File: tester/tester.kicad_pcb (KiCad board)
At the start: 2 copper layers, 29.8 x 91.4 mm, 70 parts

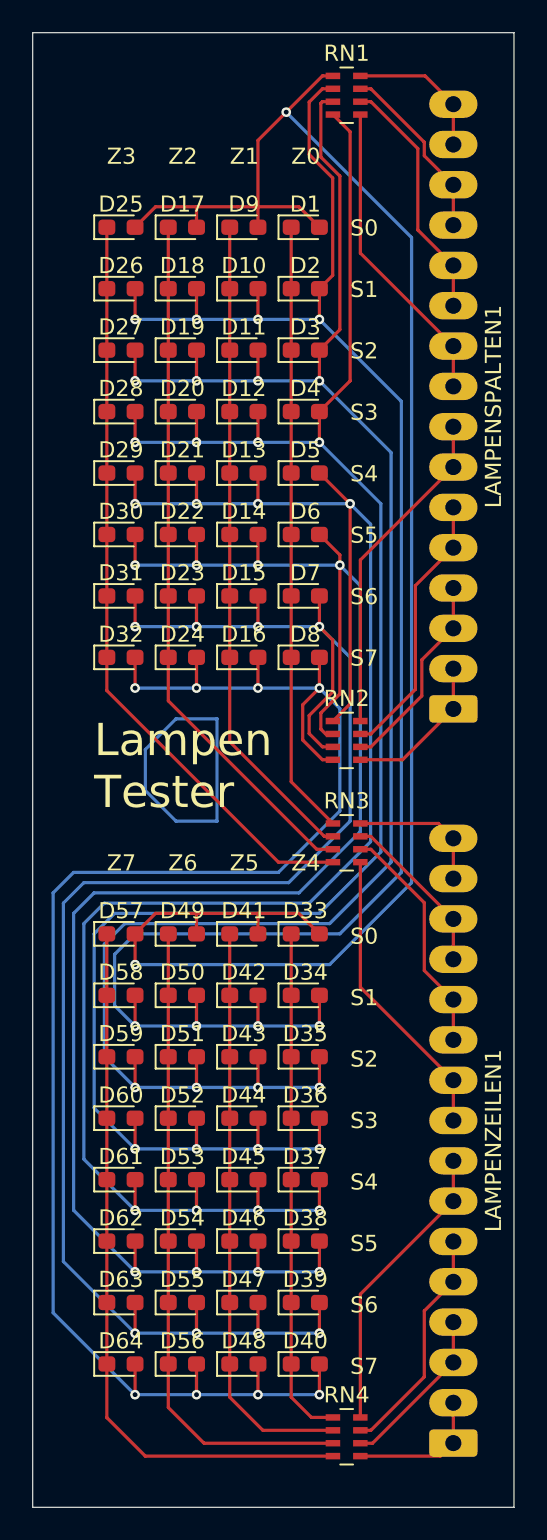
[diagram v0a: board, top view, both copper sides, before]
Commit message: led tester
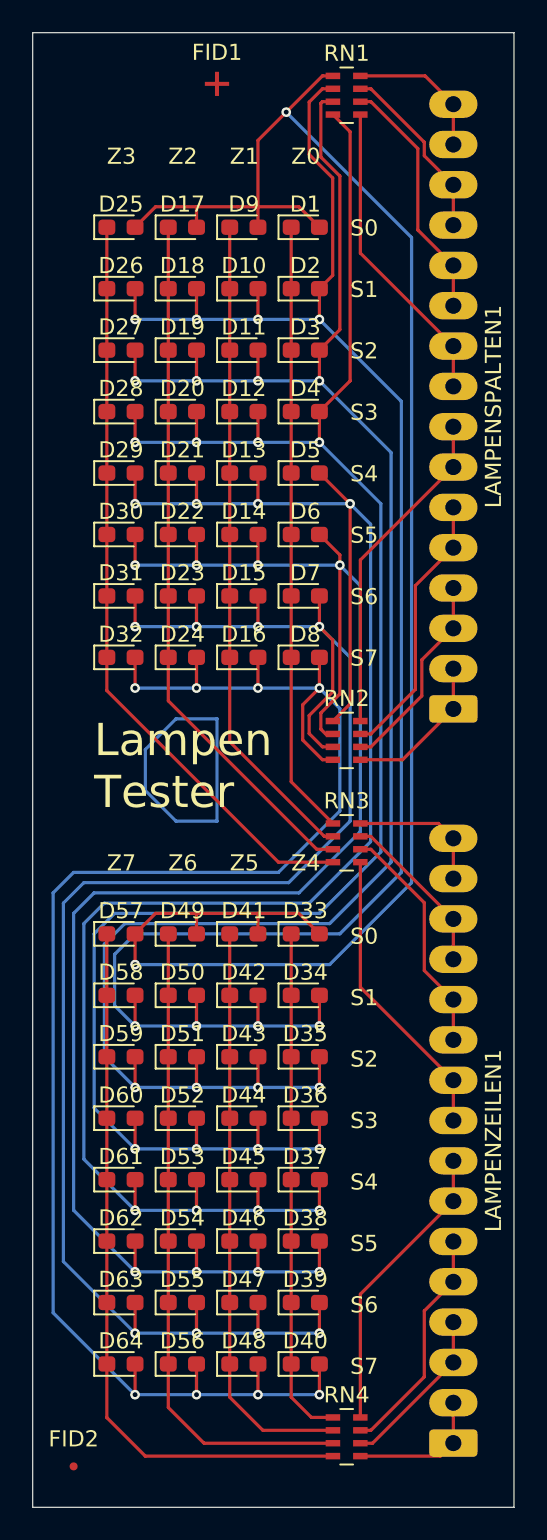
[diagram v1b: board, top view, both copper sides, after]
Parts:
- added FID1: Fiducial, Fiducial:Fiducial_Cross_1.5mm_Mask2mm, F.Cu at (49.5, 28.6)
- added FID2: Fiducial, Fiducial:Fiducial_0.5mm_Mask1.5mm, F.Cu at (40.6, 114.3)
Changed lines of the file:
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@@
 		)
+	)
+	(footprint "Fiducial:Fiducial_Cross_1.5mm_Mask2mm"
+		(layer "F.Cu")
+		(at 49.53 28.575)
+		(descr "Fiducial, cross variant, 1.5mm bare copper, 2mm soldermask opening")
+		(tags "fiducial")
+		(property "Reference" "FID1"
+			(at 0 -1.95 0)
+			(layer "F.SilkS")
+			(effects
+				(font
+					(size 1 1)
+					(thickness 0.15)
+				)
+			)
+		)
+		(property "Value" "Fiducial"
+			(at 0 1.95 0)
+			(layer "F.Fab")
+			(effects
+				(font
+					(size 1 1)
+					(thickness 0.15)
+				)
+			)
+		)
+		(property "Datasheet" "~"
+			(at 0 0 0)
+			(layer "F.Fab")
+			(hide yes)
+			(effects
+				(font
+					(size 1.27 1.27)
+					(thickness 0.15)
+				)
+			)
+		)
+		(property "Description" "Fiducial Marker"
+			(at 0 0 0)
+			(layer "F.Fab")
+			(hide yes)
+			(effects
+				(font
+					(size 1.27 1.27)
+					(thickness 0.15)
+				)
+			)
+		)
+		(property ki_fp_filters "Fiducial*")
+		(sheetname "/")
+		(sheetfile "tester.kicad_sch")
+		(attr smd exclude_from_bom)
+		(fp_circle
+			(center 0 0)
+			(end 1.25 0)
+			(stroke
+				(width 0.05)
+				(type solid)
+			)
+			(fill no)
+			(layer "F.CrtYd")
+		)
+		(fp_circle
+			(center 0 0)
+			(end 1 0)
+			(stroke
+				(width 0.1)
+				(type solid)
+			)
+			(fill no)
+			(layer "F.Fab")
+		)
+		(fp_text user "${REFERENCE}"
+			(at 0 0 0)
+			(layer "F.Fab")
+			(effects
+				(font
+					(size 0.5 0.5)
+					(thickness 0.08)
+				)
+			)
+		)
+		(pad "" smd circle
+			(at 0 0)
+			(size 0.25 0.25)
+			(layers "F.Cu" "F.Mask")
+			(solder_mask_margin 0.875)
+			(clearance 0.975)
+		)
+		(pad "" smd custom
+			(at 0 0)
+			(size 0.25 0.25)
+			(layers "F.Cu" "F.Mask")
+			(options
+				(clearance outline)
+				(anchor circle)
+			)
+			(primitives
+				(gr_rect
+					(start -0.75 -0.125)
+					(end 0.75 0.125)
+					(width 0)
+					(fill yes)
+				)
+				(gr_rect
+					(start -0.125 -0.75)
+					(end 0.125 0.75)
+					(width 0)
+					(fill yes)
+				)
+			)
+		)
+		(embedded_fonts no)
 	)
 	(footprint "LED_SMD:LED_0603_1608Metric_Pad1.05x0.95mm_HandSolder"
@@
 		)
 	)
+	(footprint "Fiducial:Fiducial_0.5mm_Mask1.5mm"
+		(layer "F.Cu")
+		(at 40.64 114.3)
+		(descr "Fiducial, circular marking, 0.5mm bare copper, 1.5mm soldermask opening")
+		(tags "fiducial")
+		(property "Reference" "FID2"
+			(at 0 -1.7 0)
+			(layer "F.SilkS")
+			(effects
+				(font
+					(size 1 1)
+					(thickness 0.15)
+				)
+			)
+		)
+		(property "Value" "Fiducial"
+			(at 0 1.7 0)
+			(layer "F.Fab")
+			(effects
+				(font
+					(size 1 1)
+					(thickness 0.15)
+				)
+			)
+		)
+		(property "Datasheet" "~"
+			(at 0 0 0)
+			(layer "F.Fab")
+			(hide yes)
+			(effects
+				(font
+					(size 1.27 1.27)
+					(thickness 0.15)
+				)
+			)
+		)
+		(property "Description" "Fiducial Marker"
+			(at 0 0 0)
+			(layer "F.Fab")
+			(hide yes)
+			(effects
+				(font
+					(size 1.27 1.27)
+					(thickness 0.15)
+				)
+			)
+		)
+		(property ki_fp_filters "Fiducial*")
+		(sheetname "/")
+		(sheetfile "tester.kicad_sch")
+		(attr smd exclude_from_bom)
+		(fp_circle
+			(center 0 0)
+			(end 1 0)
+			(stroke
+				(width 0.05)
+				(type solid)
+			)
+			(fill no)
+			(layer "F.CrtYd")
+		)
+		(fp_circle
+			(center 0 0)
+			(end 0.75 0)
+			(stroke
+				(width 0.1)
+				(type solid)
+			)
+			(fill no)
+			(layer "F.Fab")
+		)
+		(fp_text user "${REFERENCE}"
+			(at 0 0 0)
+			(layer "F.Fab")
+			(effects
+				(font
+					(size 0.38 0.38)
+					(thickness 0.06)
+				)
+			)
+		)
+		(pad "" smd circle
+			(at 0 0)
+			(size 0.5 0.5)
+			(layers "F.Cu" "F.Mask")
+			(solder_mask_margin 0.5)
+			(clearance 0.6)
+		)
+		(embedded_fonts no)
+	)
 	(footprint "LED_SMD:LED_0603_1608Metric_Pad1.05x0.95mm_HandSolder"
